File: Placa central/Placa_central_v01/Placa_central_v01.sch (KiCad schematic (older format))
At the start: 50 parts, among them J1 PinoCheckBateriaVcc, J16 Conn_01x01_Motor1PonteHPCB, J17 PinoCheckBateriaGND, J2 Conn_01x02_ArduinoTxRx, J26 Conn_02x08_Odd_Even, J27 Conn_01x01_Motor2PonteHPCB, J28 Conn_01x01_Motor1PCBMotor, J29 Conn_01x01_Motor2PCBMotor, J3 Conn_01x01_ArduinoReset, J37 Conn_01x01_8.4VPonteH, J38 Conn_01x01_5VPonteH, J39 Conn_01x01_GNDPonteH, J40 Conn_01x01_Motor1PWM, J41 Conn_01x01_Motor1Dir1, J42 Conn_01x01_Motor1Dir2, J43 Conn_01x01_Motor2Dir1, J44 Conn_01x01_Motor2Dir2, J45 Conn_01x01_Motor2PWM, J48 Conn_01x01_5VEncoderEsq, J49 Conn_01x01_OutputEncoderEsq, J50 Conn_01x01_GNDEncoderEsq, J51 Conn_01x01_5VEncoderDir, J52 Conn_01x01_OutputEncoderDir, J53 Conn_01x01_GNDEncoderDir, Q1 BC548, Q2 BC548, SW1 SW_ON/OFF, SW3 SW_comando1

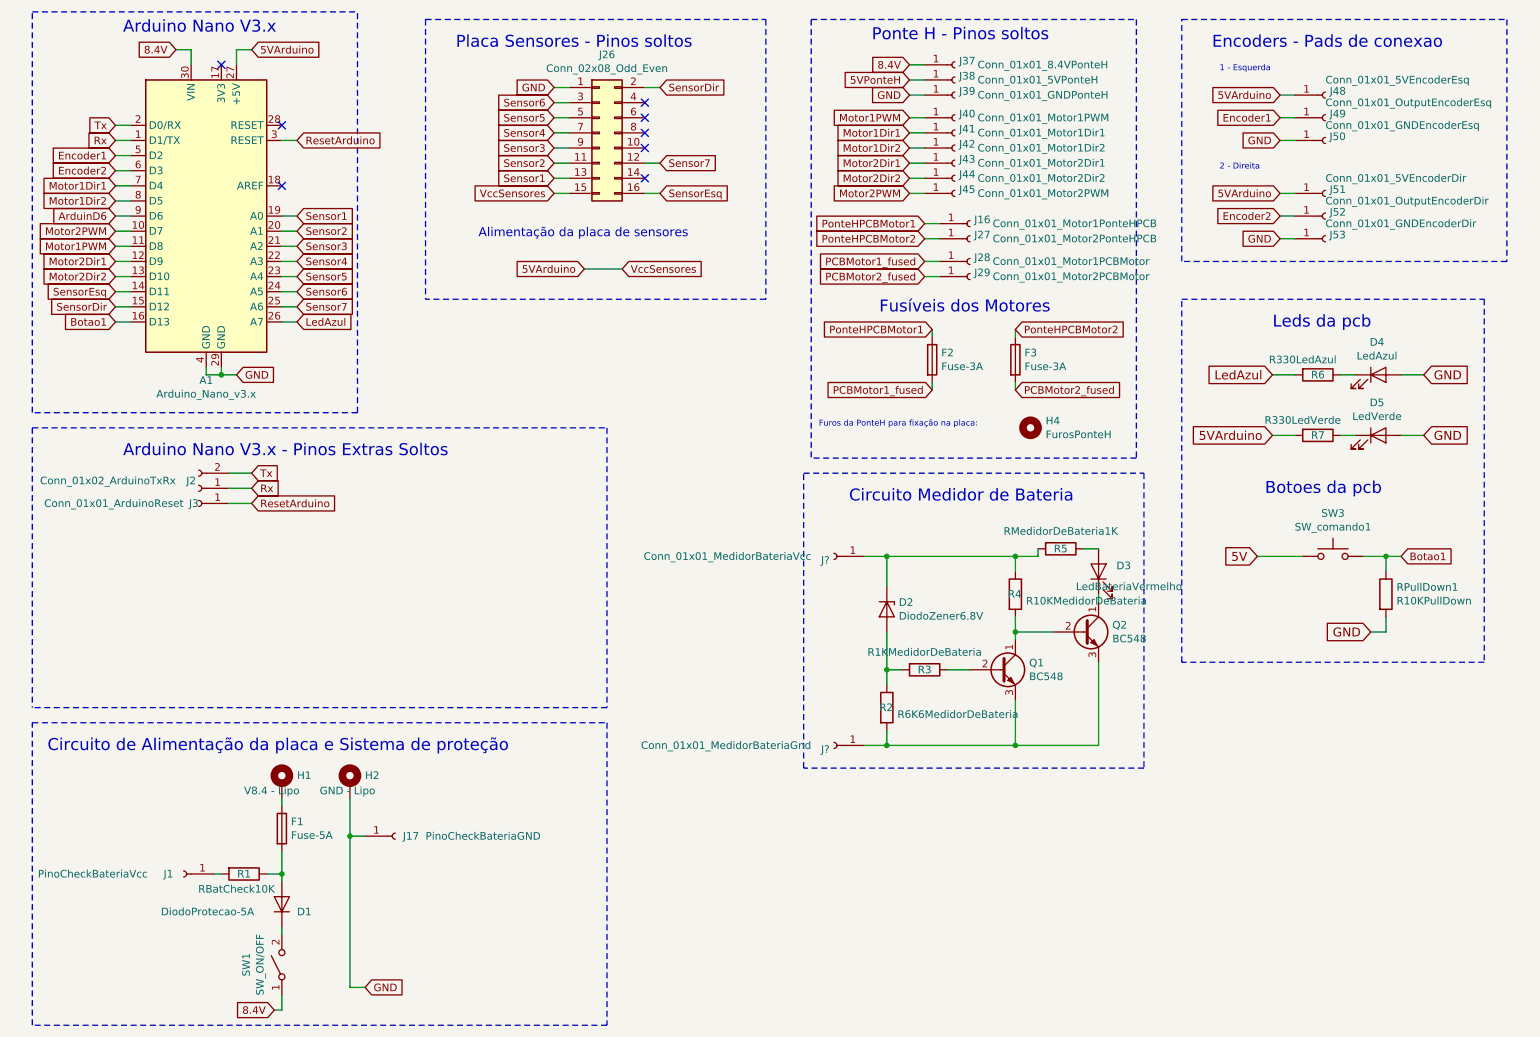
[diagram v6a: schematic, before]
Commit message: Distribuição dos compenentes praticamente concluída, quase pronta para root.
Placa Central: 5VArduino(pino 15) colocado no pino 16, enquanto o sensorEsq(pino 16) foi colocado no pino 15 para
facilitar o root; Adicionado na placa central os pads de conexao das alimentacoes provenientes do circuito de
alimentacao; Label '5V' substituída por '5VArduino' - decisão a ser revisada; Pads de solda trocados por pads maiores
por questoes de corrente alta (pinos de alimentacao). *Placa de Alimentação: Nome de dois pinos da placa de alimentação
modificados. Pads de solda trocados por pads maiores por questoes de corrente alta (pinos de alimentacao).
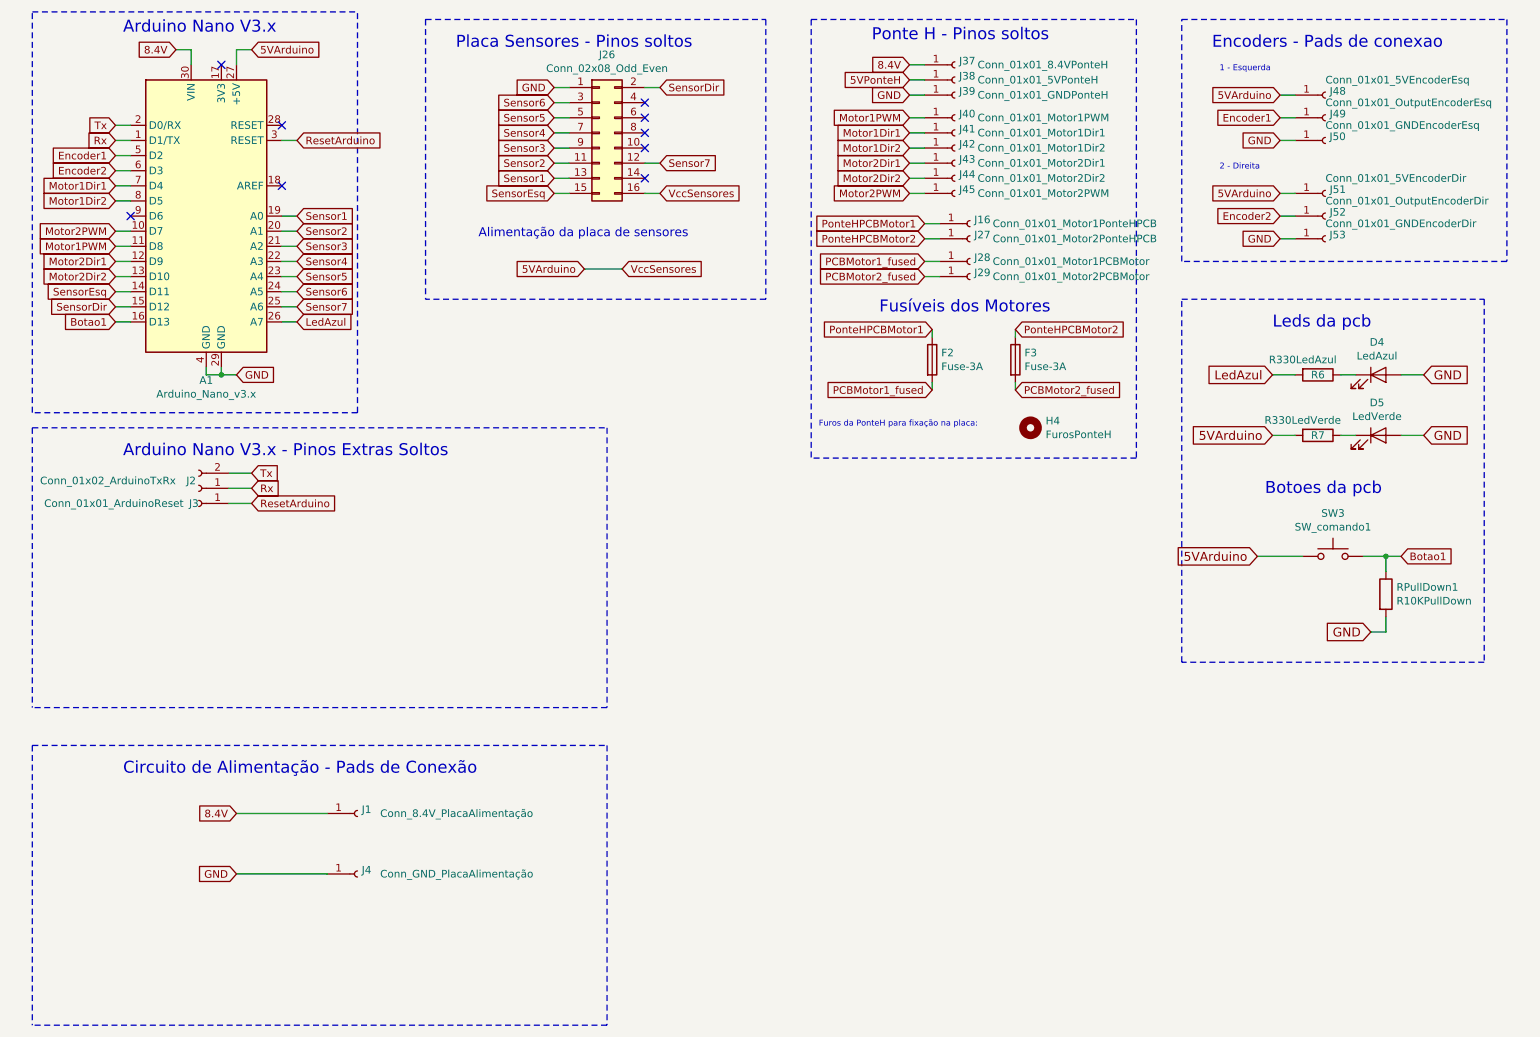
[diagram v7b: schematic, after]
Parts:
- removed D1: DiodoProtecao-5A, Diode_THT:D_DO-27_P15.24mm_Horizontal, symbol Device:D
- removed D2: DiodoZener6.8V, Diode_THT:D_DO-35_SOD27_P10.16mm_Horizontal, symbol Device:D_Zener
- removed D3: LedBateriaVermelho, LED_THT:LED_D3.0mm, symbol Device:LED
- removed F1: Fuse-5A, Fuse:Fuseholder_Cylinder-5x20mm_Stelvio-Kontek_PTF78_Horizontal_Open, symbol Device:Fuse
- removed H1: V8.4 - Lipo, Connector_Wire:SolderWirePad_1x01_Drill1.5mm, symbol Mechanical:MountingHole_Pad
- removed H2: GND - Lipo, Connector_Wire:SolderWirePad_1x01_Drill1.5mm, symbol Mechanical:MountingHole_Pad
- removed J17: PinoCheckBateriaGND, Connector_Wire:SolderWirePad_1x01_Drill1.5mm, symbol Connector:Conn_01x01_Female
- removed J?: Conn_01x01_MedidorBateriaVcc, Connector_PinSocket_2.54mm:PinSocket_1x01_P2.54mm_Vertical, symbol Connector:Conn_01x01_Female
- removed J?: Conn_01x01_MedidorBateriaGnd, Connector_PinSocket_2.54mm:PinSocket_1x01_P2.54mm_Vertical, symbol Connector:Conn_01x01_Female
- removed Q1, Q2: BC548, Package_TO_SOT_THT:TO-92_Wide, symbol Transistor_BJT:BC548
- removed R1: RBatCheck10K, Resistor_THT:R_Axial_DIN0207_L6.3mm_D2.5mm_P10.16mm_Horizontal, symbol Device:R
- removed R2: R6K6MedidorDeBateria, Resistor_THT:R_Axial_DIN0207_L6.3mm_D2.5mm_P10.16mm_Horizontal, symbol Device:R
- removed R3: R1KMedidorDeBateria, Resistor_THT:R_Axial_DIN0207_L6.3mm_D2.5mm_P10.16mm_Horizontal, symbol Device:R
- removed R4: R10KMedidorDeBateria, Resistor_THT:R_Axial_DIN0207_L6.3mm_D2.5mm_P10.16mm_Horizontal, symbol Device:R
- removed R5: RMedidorDeBateria1K, Resistor_THT:R_Axial_DIN0207_L6.3mm_D2.5mm_P10.16mm_Horizontal, symbol Device:R
- removed SW1: SW_ON/OFF, CUSTOM_Placa_central_v01:Solder_Pad_Custom, symbol Switch:SW_SPST
- added J4: Conn_GND_PlacaAlimentação, Connector_Wire:SolderWirePad_1x01_Drill1.2mm, symbol Connector:Conn_01x01_Female
- J1: value PinoCheckBateriaVcc -> Conn_8.4V_PlacaAlimentação; footprint Connector_PinSocket_2.54mm:PinSocket_1x01_P2.54mm_Vertical -> Connector_Wire:SolderWirePad_1x01_Drill1.2mm
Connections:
- net 5V is gone; now on net 5VArduino: SW3.1
- net 5VArduino: now also J26.16 (Pin_16); no longer J26.15 (Pin_15)
- net 8.4V: now also J1.1 (Pin_1)
- net GND: now also J4.1 (Pin_1)
- net SensorEsq: now also J26.15 (Pin_15); no longer J26.16 (Pin_16)
- net ArduinD6: no longer names the net of A1.9 (D6)
- no-connect marks 8 -> 9
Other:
- note added: "Circuito de Alimentação - Pads de Conexão"
- note removed: "Circuito Medidor de Bateria"
- note removed: "Circuito de Alimentação da placa e Sistema de proteção"

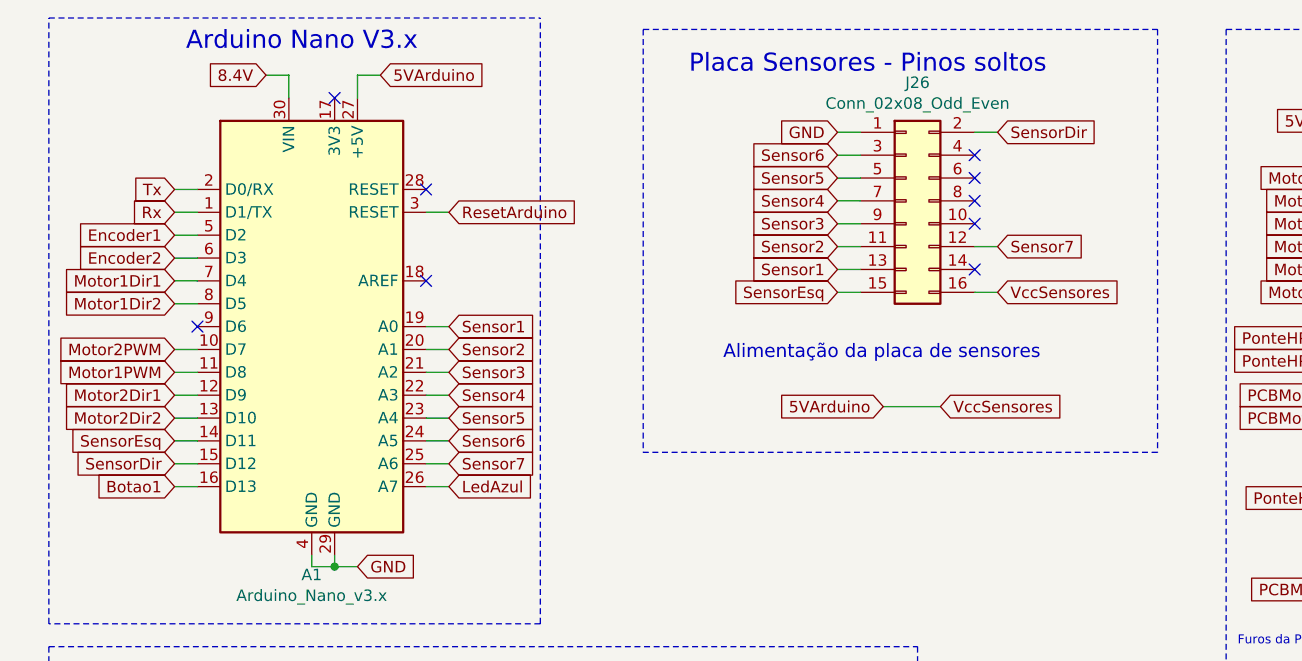
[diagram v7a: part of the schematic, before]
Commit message: Root finalizado, aguardando revisão dos demais membros. Ocorreram mudanças massivas nas conexões de pinos lógicos e do conector.
Track Width (grossura da linha) modificado para 0,9 mm na placa central. Conexões do Conector rearranjadas.
Tag 'Botão1' movida para o pino 6;
Tag 'Arduino13' (agora vago - pino 16) adicionado ao conector;
Pino ArduinoD13 será adicionado ao conector (se possível), para possível uso futuro. Outros pinos extras não serão adicionados. O pino será de fato adicionado na PBC dos sensores.
Tag 'Motor1Pwm' movida para o pino 13;
Tag 'Motor2Dir2' movida para o pino 12;
Tag 'Motor2Dir1' movida para pino 11;
Tag 'Motor1Dir1' movida para o pino 10;
Tag 'Encoder2' movida para o pino 7;
Tag 'Motor2PWM' movida para o pino 8;
Tag 'Motor1Dir2' movida para o pino 9;
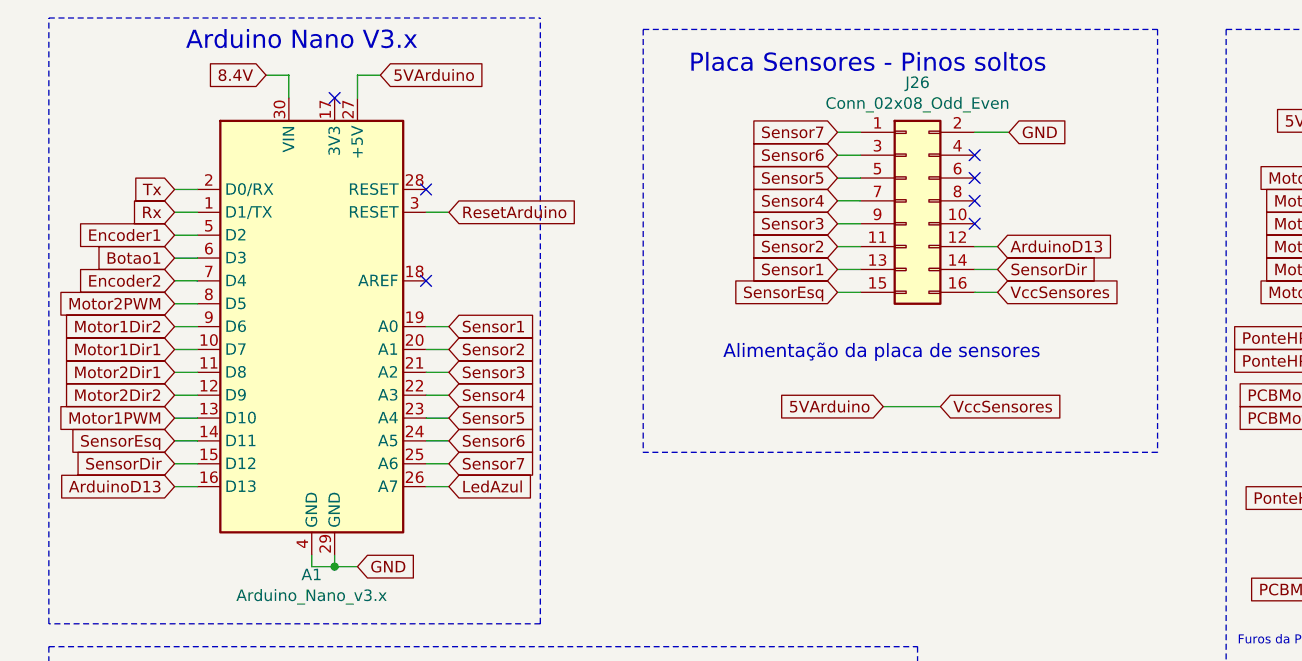
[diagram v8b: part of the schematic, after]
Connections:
- net Botao1: now also A1.6 (D3); no longer A1.16 (D13)
- net Encoder2: now also A1.7 (D4); no longer A1.6 (D3)
- net GND: now also J26.2 (Pin_2); no longer J26.1 (Pin_1)
- net Motor1Dir1: now also A1.10 (D7); no longer A1.7 (D4)
- net Motor1Dir2: now also A1.9 (D6); no longer A1.8 (D5)
- net Motor1PWM: now also A1.13 (D10); no longer A1.11 (D8)
- net Motor2Dir1: now also A1.11 (D8); no longer A1.12 (D9)
- net Motor2Dir2: now also A1.12 (D9); no longer A1.13 (D10)
- net Motor2PWM: now also A1.8 (D5); no longer A1.10 (D7)
- net Sensor7: now also J26.1 (Pin_1); no longer J26.12 (Pin_12)
- net SensorDir: now also J26.14 (Pin_14); no longer J26.2 (Pin_2)
- new net ArduinoD13: A1.16 (D13), J26.12 (Pin_12)
- no-connect marks 9 -> 7
